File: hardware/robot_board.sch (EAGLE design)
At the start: 135 parts, among them J1 POWER_JACKPTH, Q1 DMP2035U, Q2 DMP2035U, Q3 DMP2035U-7, Q4 DMP2035U-7, U1 FT232RL-BASICSSOP, U11 LM393, U12 LM393, U16 LM393, U17 ATMEGA325PA, U2 SIA907EDJT, U3 MIC5219, U5 SIA907EDJT, U6 SIA907EDJT, U7 TLV70233, Y1 16MHz

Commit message: more routing
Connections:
- net 5V: no longer JP6.1, JP6.2, JP6.3, JP6.4
- net VIN_F: now also JP6.1, JP6.2, JP6.3, JP6.4

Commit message: added Bluetooth module
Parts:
- removed U$9: M08X2, SparkFun-Connectors:M08X2
- added U$1: M08X2, SparkFun-Connectors:M08X2
- added U4: HC_05, SerialPortBluetooth:HC_05
- D1, D10, D11, D12, D13, D14, D15, D16, D17, D18, D19, D2, D20, D21, D22, D26, D27, D28, D29, D3, D4, D5, D6, D7, D8, D9: value (none) -> 5.1V
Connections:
- removed net LCD_E: U17.PG4
- removed net LCD_RS: U17.PG3
- removed net N$47: U$9.3
- removed net N$48: U$9.5
- removed net N$59: U$9.6
- removed net N$60: U$9.4
- new net E: U$1.8, U17.PC0
- new net IR: IR.1, U17.PD0
- new net RS: U$1.6, U17.PC1
- net 5V: now also IR.2, U$1.2, U$1.4, U$1.5; no longer U$9.2
- net GND: now also IR.3, U$1.1, U$1.3, U$1.7; no longer U$9.1
- net LCD0: now also U$1.9; no longer U$9.7
- net LCD1: now also U$1.10; no longer U$9.8
- net LCD2: now also U$1.11; no longer U$9.9
- net LCD3: now also U$1.12; no longer U$9.10
- net LCD4: now also U$1.13; no longer U$9.11
- net LCD5: now also U$1.14; no longer U$9.12
- net LCD6: now also U$1.15; no longer U$9.13
- net LCD7: now also U$1.16; no longer U$9.14
- net SW1: now also U17.PE7
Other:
- note added: "Vin 3-10V"

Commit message: reversed digital/analog pins
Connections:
- net 5V: no longer IR.2
- net 5V_UC: now also IR.2
- net D7_IN: now also U17.PC5
- net D8_IN: now also U17.PC6
- net D9_IN: now also U17.PC7
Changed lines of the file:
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@@
 <label x="91.44" y="38.1" size="1.778" layer="95"/>
+</segment>
+<segment>
+<pinref part="IR" gate="G$1" pin="2"/>
+<wire x1="335.28" y1="81.28" x2="332.74" y2="81.28" width="0.1524" layer="91"/>
+<label x="332.74" y="81.28" size="1.778" layer="95"/>
 </segment>
 </net>
@@
 <junction x="261.62" y="86.36"/>
 </segment>
+<segment>
+<pinref part="U17" gate="G$1" pin="PC6"/>
+<wire x1="154.94" y1="15.24" x2="160.02" y2="15.24" width="0.1524" layer="91"/>
+<label x="154.94" y="15.24" size="1.778" layer="95"/>
+</segment>
 </net>
 <net name="D9_IN" class="0">
@@
 <junction x="261.62" y="76.2"/>
 </segment>
+<segment>
+<pinref part="U17" gate="G$1" pin="PC7"/>
+<wire x1="154.94" y1="17.78" x2="160.02" y2="17.78" width="0.1524" layer="91"/>
+<label x="154.94" y="17.78" size="1.778" layer="95"/>
+</segment>
 </net>
 <net name="D2_IN" class="0">
@@
 <label x="246.38" y="-50.8" size="1.778" layer="95"/>
 <junction x="261.62" y="-50.8"/>
+</segment>
+<segment>
+<pinref part="U17" gate="G$1" pin="PC5"/>
+<wire x1="154.94" y1="12.7" x2="160.02" y2="12.7" width="0.1524" layer="91"/>
+<label x="154.94" y="12.7" size="1.778" layer="95"/>
 </segment>
 </net>
@@
 <pinref part="U$1" gate="G$1" pin="5"/>
 </segment>
-<segment>
-<pinref part="IR" gate="G$1" pin="2"/>
-<wire x1="335.28" y1="81.28" x2="332.74" y2="81.28" width="0.1524" layer="91"/>
-<label x="332.74" y="81.28" size="1.778" layer="95"/>
-</segment>
-</net>
+</net>

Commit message: updated bluetooth
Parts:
- added C6: .1uF, resistor:C-USC1206
- added C7: 22uF, resistor:C-USC1206
- added D24: POWER, SparkFun-LED:LED-GREENLILYPAD
- added D32: 5.1V, SparkFun-DiscreteSemi:DIODESOT23
- added D33: BAT54C, diode:BAT54C
- added R57: 330, resistor:R-US_R1206
- added R58, R60: 300K, resistor:R-US_R1206
- added R59, R61: 1K, resistor:R-US_R1206
- added R62: 2K, resistor:R-US_R1206
- R23, R27, R28, R35, R45, R46: value (none) -> 10K
- R24: value (none) -> 12K
- R26: value (none) -> 7.68K
- R29, R31: value (none) -> 15K
- R36: value (none) -> 20K
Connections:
- removed net N$31: U$6.FAULT
- new net AREF_IN: D32.C, R59.1, U17.AREF
- new net N$10: D24.A, U1.RXLED
- new net N$11: D24.C, R57.2
- new net N$12: D33.CC, R42.2
- new net N$14: R61.2, U4.TX
- net 3V3: now also C7.1, U4.3V3; no longer R30.2
- net 3V3_OUT: now also R30.2
- net 5V: now also C6.1; no longer R25.2
- net 5VREG_SWO: now also R58.1
- net 5V_OUT: now also JP10.3, JP10.4, JP11.3, JP11.4, R25.2
- net A0: now also JP10.1
- net A1: now also JP10.2
- net AREF: now also R59.2; no longer U17.AREF
- net D0: now also JP11.1
- net D0_IN: now also R61.1, R62.2
- net D1: now also JP11.2
- net D1_IN: now also U4.RX
- net GND: now also C6.2, C7.2, D32.A, JP10.5, JP10.6, JP11.5, JP11.6, R57.1, R60.1, R62.1, U4.GND, U4.GND2
- net N$35: now also R58.2
- net PWR_SW: now also D33.A1
- net USBGATE: now also R60.2
- net USB_5V: now also D33.A2
- net VIN_F: no longer R42.2
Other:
- moved on the sheet: JP10, R25, R30, R42

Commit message: updated Bluetooth pinout
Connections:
- new net BT_RX: U17.PE3, U4.RX
- new net BT_TX: R61.1, R62.2, U17.PE2
- net D0_IN: no longer R61.1, R62.2
- net D1_IN: no longer U4.RX
- net D2_IN: now also U17.PG3; no longer U17.PE2
- net D3_IN: now also U17.PG4; no longer U17.PE3
- net GND: now also U$4.GND_PPAD, U$5.GND_PPAD, U4.PIO11
- net N$28: now also U2.D1@, U2.D2@
- net N$42: now also U6.D1@, U6.D2@
- net N$44: now also U5.D1@, U5.D2@
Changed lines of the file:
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@@
 <label x="381" y="10.16" size="1.778" layer="95"/>
+</segment>
+<segment>
+<pinref part="U$5" gate="G$1" pin="GND_PPAD"/>
+<wire x1="330.2" y1="147.32" x2="335.28" y2="147.32" width="0.1524" layer="91"/>
+<label x="332.74" y="147.32" size="1.778" layer="95"/>
+</segment>
+<segment>
+<pinref part="U$4" gate="G$1" pin="GND_PPAD"/>
+<wire x1="266.7" y1="147.32" x2="266.7" y2="142.24" width="0.1524" layer="91"/>
+<label x="266.7" y="142.24" size="1.778" layer="95"/>
+</segment>
+<segment>
+<pinref part="U4" gate="G$1" pin="PIO11"/>
+<wire x1="381" y1="40.64" x2="383.54" y2="40.64" width="0.1524" layer="91"/>
+<label x="381" y="40.64" size="1.778" layer="95"/>
 </segment>
 </net>
@@
 </segment>
 <segment>
-<pinref part="U17" gate="G$1" pin="PE2"/>
-<wire x1="111.76" y1="66.04" x2="106.68" y2="66.04" width="0.1524" layer="91"/>
-<label x="106.68" y="66.04" size="1.778" layer="95"/>
+<pinref part="U17" gate="G$1" pin="PG3"/>
+<wire x1="111.76" y1="30.48" x2="106.68" y2="30.48" width="0.1524" layer="91"/>
+<label x="106.68" y="30.48" size="1.778" layer="95"/>
 </segment>
 </net>
@@
 </segment>
 <segment>
-<pinref part="U17" gate="G$1" pin="PE3"/>
-<wire x1="111.76" y1="63.5" x2="106.68" y2="63.5" width="0.1524" layer="91"/>
-<label x="106.68" y="63.5" size="1.778" layer="95"/>
+<pinref part="U17" gate="G$1" pin="PG4"/>
+<wire x1="111.76" y1="27.94" x2="106.68" y2="27.94" width="0.1524" layer="91"/>
+<label x="106.68" y="27.94" size="1.778" layer="95"/>
 </segment>
 </net>
@@
 <wire x1="60.96" y1="132.08" x2="60.96" y2="114.3" width="0.1524" layer="91"/>
 <pinref part="U6" gate="G$1" pin="D2"/>
-<wire x1="60.96" y1="114.3" x2="76.2" y2="114.3" width="0.1524" layer="91"/>
+<wire x1="60.96" y1="114.3" x2="71.12" y2="114.3" width="0.1524" layer="91"/>
+<pinref part="U6" gate="G$1" pin="D1@"/>
+<wire x1="71.12" y1="114.3" x2="76.2" y2="114.3" width="0.1524" layer="91"/>
+<wire x1="76.2" y1="111.76" x2="73.66" y2="111.76" width="0.1524" layer="91"/>
+<wire x1="73.66" y1="111.76" x2="71.12" y2="111.76" width="0.1524" layer="91"/>
+<wire x1="71.12" y1="111.76" x2="71.12" y2="114.3" width="0.1524" layer="91"/>
+<pinref part="U6" gate="G$1" pin="D2@"/>
+<wire x1="99.06" y1="109.22" x2="99.06" y2="106.68" width="0.1524" layer="91"/>
+<wire x1="99.06" y1="106.68" x2="73.66" y2="106.68" width="0.1524" layer="91"/>
+<wire x1="73.66" y1="106.68" x2="73.66" y2="111.76" width="0.1524" layer="91"/>
+<junction x="71.12" y="114.3"/>
+<junction x="73.66" y="111.76"/>
 </segment>
 </net>
@@
 <pinref part="U5" gate="G$1" pin="D1"/>
 <wire x1="50.8" y1="86.36" x2="66.04" y2="86.36" width="0.1524" layer="91"/>
-<wire x1="66.04" y1="86.36" x2="66.04" y2="71.12" width="0.1524" layer="91"/>
+<wire x1="66.04" y1="86.36" x2="66.04" y2="68.58" width="0.1524" layer="91"/>
+<wire x1="66.04" y1="68.58" x2="50.8" y2="68.58" width="0.1524" layer="91"/>
+<wire x1="50.8" y1="68.58" x2="27.94" y2="68.58" width="0.1524" layer="91"/>
+<wire x1="27.94" y1="68.58" x2="22.86" y2="68.58" width="0.1524" layer="91"/>
+<wire x1="22.86" y1="68.58" x2="22.86" y2="76.2" width="0.1524" layer="91"/>
 <pinref part="U5" gate="G$1" pin="D2"/>
-<wire x1="66.04" y1="71.12" x2="27.94" y2="71.12" width="0.1524" layer="91"/>
-<wire x1="27.94" y1="71.12" x2="27.94" y2="76.2" width="0.1524" layer="91"/>
+<wire x1="22.86" y1="76.2" x2="27.94" y2="76.2" width="0.1524" layer="91"/>
+<pinref part="U5" gate="G$1" pin="D1@"/>
+<wire x1="27.94" y1="73.66" x2="27.94" y2="68.58" width="0.1524" layer="91"/>
+<pinref part="U5" gate="G$1" pin="D2@"/>
+<wire x1="50.8" y1="71.12" x2="50.8" y2="68.58" width="0.1524" layer="91"/>
+<junction x="50.8" y="68.58"/>
+<junction x="27.94" y="68.58"/>
 </segment>
 </net>
@@
 <net name="N$28" class="0">
 <segment>
-<pinref part="U2" gate="G$1" pin="D2"/>
-<wire x1="43.18" y1="22.86" x2="43.18" y2="17.78" width="0.1524" layer="91"/>
-<wire x1="43.18" y1="17.78" x2="76.2" y2="17.78" width="0.1524" layer="91"/>
-<wire x1="76.2" y1="17.78" x2="76.2" y2="33.02" width="0.1524" layer="91"/>
+<wire x1="40.64" y1="15.24" x2="66.04" y2="15.24" width="0.1524" layer="91"/>
+<wire x1="66.04" y1="15.24" x2="76.2" y2="15.24" width="0.1524" layer="91"/>
+<wire x1="76.2" y1="15.24" x2="76.2" y2="33.02" width="0.1524" layer="91"/>
 <pinref part="U2" gate="G$1" pin="D1"/>
 <wire x1="76.2" y1="33.02" x2="66.04" y2="33.02" width="0.1524" layer="91"/>
+<pinref part="U2" gate="G$1" pin="D2@"/>
+<wire x1="66.04" y1="15.24" x2="66.04" y2="17.78" width="0.1524" layer="91"/>
+<pinref part="U2" gate="G$1" pin="D2"/>
+<wire x1="43.18" y1="22.86" x2="40.64" y2="22.86" width="0.1524" layer="91"/>
+<wire x1="40.64" y1="22.86" x2="40.64" y2="20.32" width="0.1524" layer="91"/>
+<pinref part="U2" gate="G$1" pin="D1@"/>
+<wire x1="40.64" y1="20.32" x2="40.64" y2="15.24" width="0.1524" layer="91"/>
+<wire x1="43.18" y1="20.32" x2="40.64" y2="20.32" width="0.1524" layer="91"/>
+<junction x="40.64" y="20.32"/>
+<junction x="66.04" y="15.24"/>
 </segment>
 </net>
@@
 <junction x="261.62" y="5.08"/>
 </segment>
-<segment>
-<pinref part="R61" gate="G$1" pin="1"/>
-<pinref part="R62" gate="G$1" pin="2"/>
-<wire x1="320.04" y1="27.94" x2="320.04" y2="30.48" width="0.1524" layer="91"/>
-<wire x1="320.04" y1="30.48" x2="317.5" y2="30.48" width="0.1524" layer="91"/>
-<label x="312.42" y="27.94" size="1.778" layer="95"/>
-</segment>
 </net>
 <net name="D1_IN" class="0">
@@
 <label x="246.38" y="-5.08" size="1.778" layer="95"/>
 <junction x="261.62" y="-5.08"/>
-</segment>
-<segment>
-<pinref part="U4" gate="G$1" pin="RX"/>
-<wire x1="332.74" y1="38.1" x2="330.2" y2="38.1" width="0.1524" layer="91"/>
-<label x="325.12" y="38.1" size="1.778" layer="95"/>
 </segment>
 </net>
@@
 </segment>
 </net>
+<net name="BT_TX" class="0">
+<segment>
+<pinref part="U17" gate="G$1" pin="PE2"/>
+<wire x1="111.76" y1="66.04" x2="106.68" y2="66.04" width="0.1524" layer="91"/>
+<label x="106.68" y="66.04" size="1.778" layer="95"/>
+</segment>
+<segment>
+<pinref part="R61" gate="G$1" pin="1"/>
+<pinref part="R62" gate="G$1" pin="2"/>
+<wire x1="320.04" y1="27.94" x2="320.04" y2="30.48" width="0.1524" layer="91"/>
+<wire x1="320.04" y1="30.48" x2="317.5" y2="30.48" width="0.1524" layer="91"/>
+<label x="312.42" y="27.94" size="1.778" layer="95"/>
+<junction x="320.04" y="30.48"/>
+</segment>
+</net>
+<net name="BT_RX" class="0">
+<segment>
+<pinref part="U17" gate="G$1" pin="PE3"/>
+<wire x1="111.76" y1="63.5" x2="106.68" y2="63.5" width="0.1524" layer="91"/>
+<label x="106.68" y="63.5" size="1.778" layer="95"/>
+</segment>
+<segment>
+<pinref part="U4" gate="G$1" pin="RX"/>
+<wire x1="332.74" y1="38.1" x2="330.2" y2="38.1" width="0.1524" layer="91"/>
+<label x="325.12" y="38.1" size="1.778" layer="95"/>
+</segment>
+</net>

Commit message: updated routing
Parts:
- removed D24: POWER, SparkFun-LED:LED-GREENLILYPAD
- added C8: .1uF, resistor:C-USC1206
- added C9: 1uF, resistor:C-USC1206
- added D34: POWER, SparkFun-LED:LED-GREENLILYPAD
- added R63: 1K, resistor:R-US_R1206
- added U$2: POT, r_cubed:POT
- D23: value 2.1V -> 2.4V; device diode:ZENER-DIODESOD80C -> SparkFun-DiscreteSemi:DIODESOT23
- R24: value 12K -> 12K 1%
- R26: value 7.68K -> 7.68K 1%
- R27, R28, R45, R46: value 10K -> 10K 1%
- R29, R31: value 15K -> 15K 1%
- R58: value 300K -> 300K 1%
- renumbered S1 to RESET, U$4 to U9, U$5 to U10, U$6 to U8
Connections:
- new net N$13: R61.1, R62.2, U4.RX
- new net N$15: U$1.5, U$2.S
- net 3V3: now also C9.1
- net 5V: now also R57.1, U$2.A; no longer U$1.5
- net 5V_UC: now also C8.1
- net BT_RX: now also R61.2; no longer U4.RX
- net BT_TX: now also U4.TX; no longer R61.1, R62.2
- net DTR: now also R63.1; no longer U1.DTR
- net GND: now also C8.2, C9.2, U$2.E, U1.TEST; no longer R57.1
- net N$10: now also D34.C; no longer D24.A
- net N$11: now also D34.A; no longer D24.C
- net N$14: now also R63.2, U1.DTR; no longer R61.2, U4.TX
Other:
- moved on the sheet: R39, R53, R57

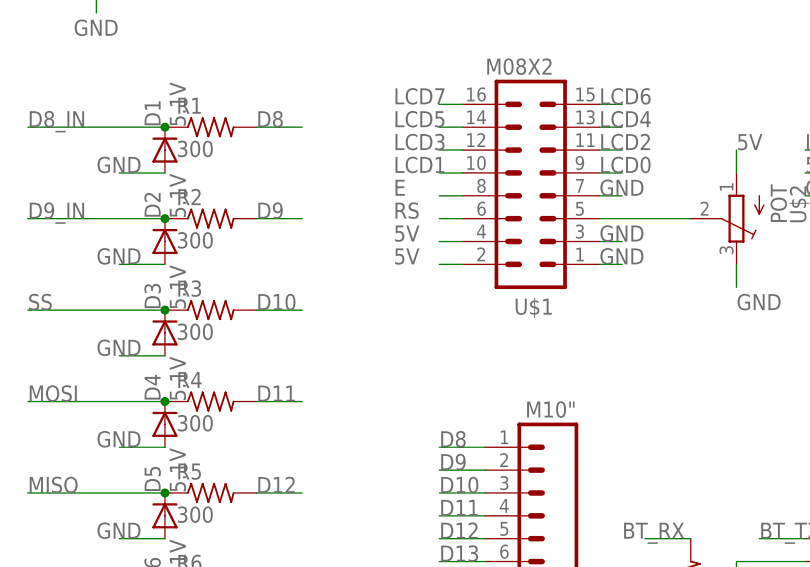
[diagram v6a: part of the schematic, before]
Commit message: fix analog pin ordering error
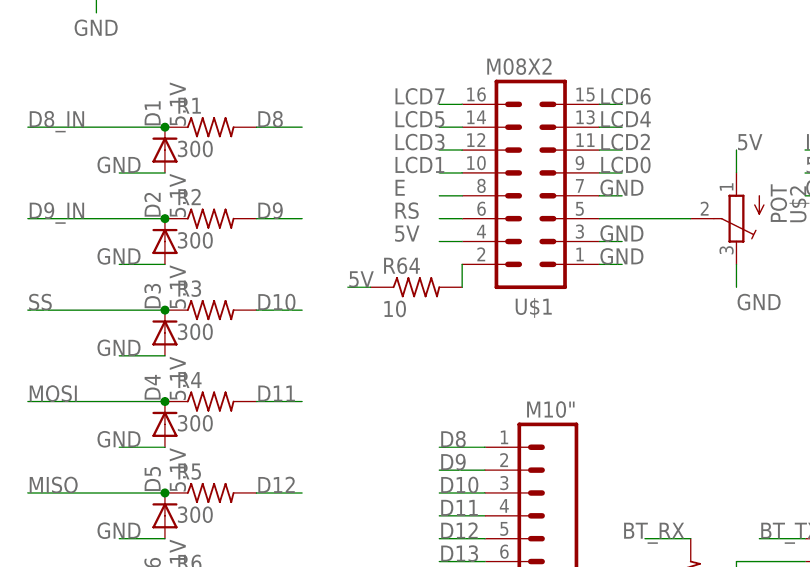
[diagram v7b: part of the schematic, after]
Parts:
- added R64: 10, resistor:R-US_R1206
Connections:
- new net N$16: R64.2, U$1.2
- net 5V: now also R64.1; no longer U$1.2
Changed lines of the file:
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@@
 <part name="U$2" library="r_cubed" deviceset="POT" device=""/>
 <part name="D34" library="SparkFun-LED" deviceset="LED-GREEN" device="LILYPAD" value="POWER"/>
+<part name="R64" library="resistor" deviceset="R-US_" device="R1206" value="10"/>
 </parts>
 <sheets>
@@
 <instance part="U$2" gate="G$1" x="325.12" y="76.2" rot="R180"/>
 <instance part="D34" gate="G$1" x="228.6" y="139.7" rot="R270"/>
+<instance part="R64" gate="G$1" x="289.56" y="68.58"/>
 </instances>
 <busses>
@@
 </segment>
 <segment>
-<pinref part="U$1" gate="G$1" pin="2"/>
-<wire x1="294.64" y1="71.12" x2="292.1" y2="71.12" width="0.1524" layer="91"/>
-<label x="287.02" y="71.12" size="1.778" layer="95"/>
-</segment>
-<segment>
 <pinref part="C6" gate="G$1" pin="1"/>
 <wire x1="294.64" y1="193.04" x2="294.64" y2="195.58" width="0.1524" layer="91"/>
@@
 <wire x1="243.84" y1="139.7" x2="246.38" y2="139.7" width="0.1524" layer="91"/>
 <label x="243.84" y="139.7" size="1.778" layer="95"/>
+</segment>
+<segment>
+<pinref part="R64" gate="G$1" pin="1"/>
+<wire x1="284.48" y1="68.58" x2="281.94" y2="68.58" width="0.1524" layer="91"/>
+<label x="281.94" y="68.58" size="1.778" layer="95"/>
 </segment>
 </net>
@@
 </segment>
 </net>
+<net name="N$16" class="0">
+<segment>
+<pinref part="U$1" gate="G$1" pin="2"/>
+<pinref part="R64" gate="G$1" pin="2"/>
+<wire x1="294.64" y1="71.12" x2="294.64" y2="68.58" width="0.1524" layer="91"/>
+</segment>
+</net>
